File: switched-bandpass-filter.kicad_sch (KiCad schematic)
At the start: 12 parts, among them J1 SMA, J10 F3 out, J11 F4 out, J2 SMA, J3 F4 in, J4 Conn_01x06_Pin, J5 F3 in, J6 F2 in, J7 F1 in, J8 F1 out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

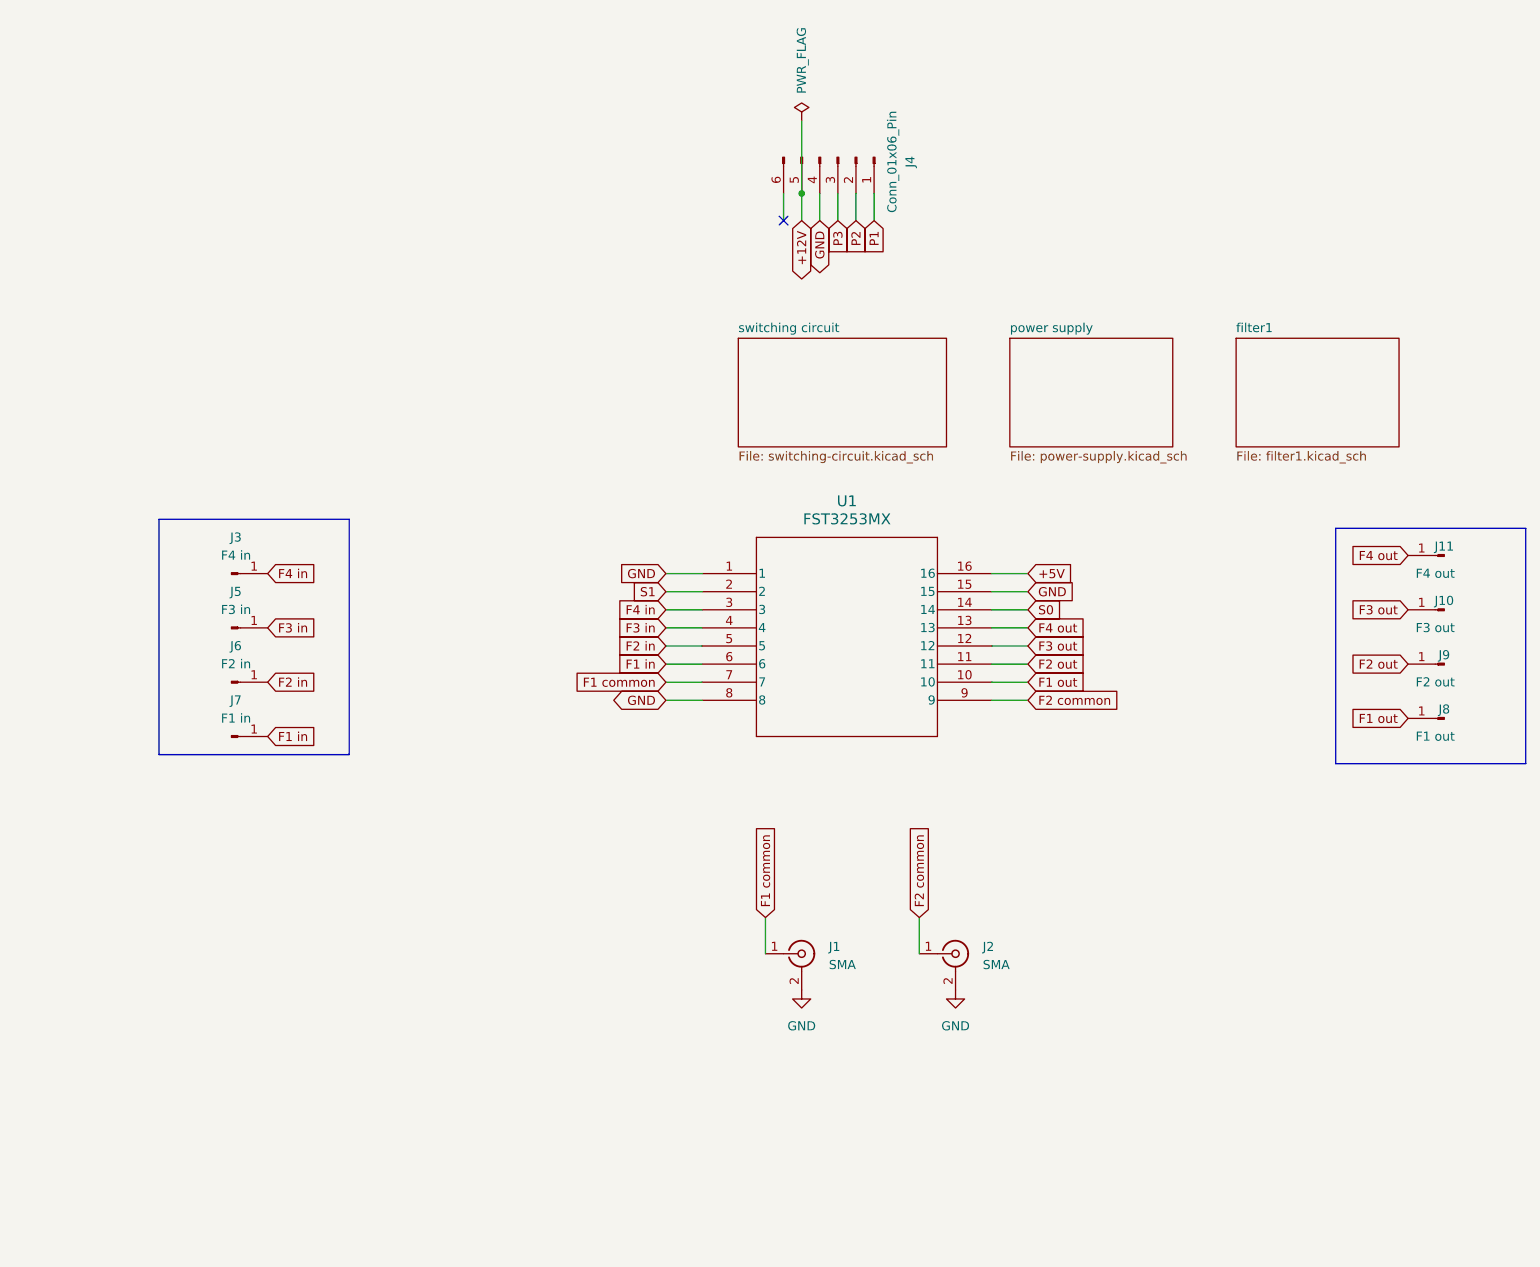
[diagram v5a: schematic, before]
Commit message: v0.4 ERC/DRC pass; added missing caps; mounting holes; moved SMA & headers out and re-spaced filter chains
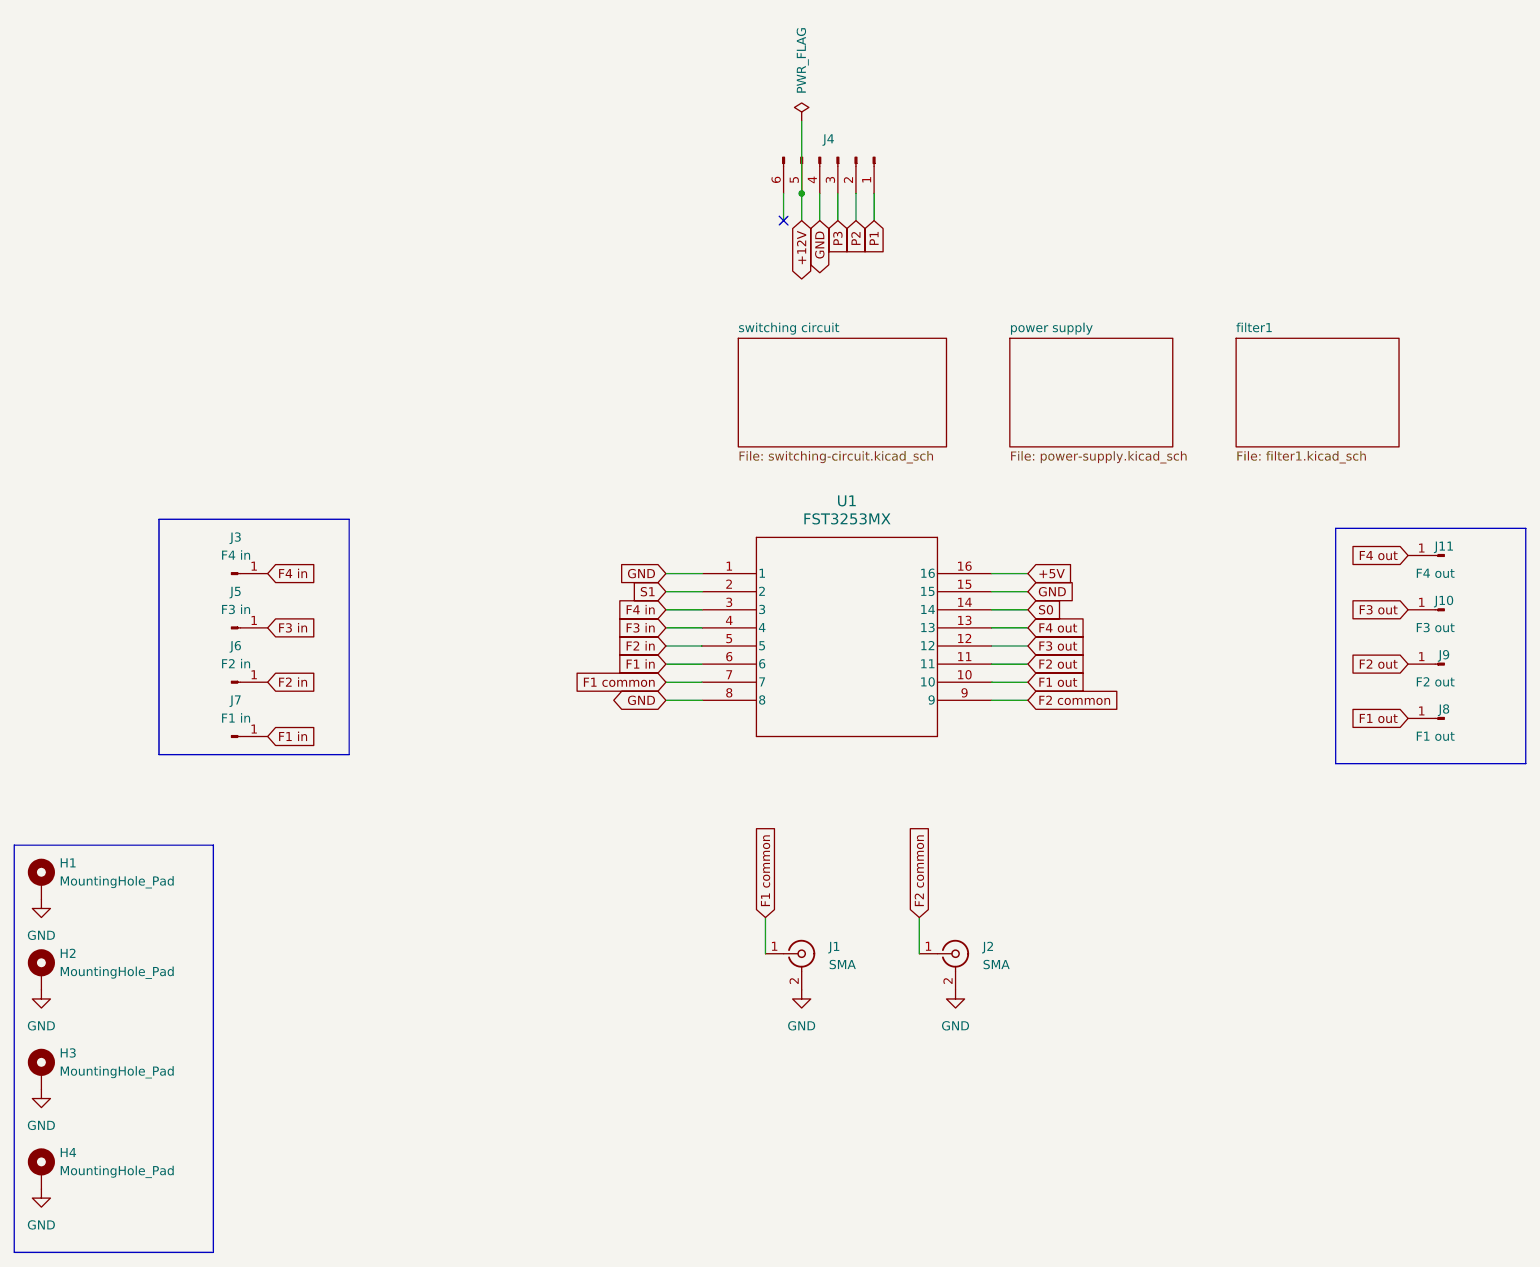
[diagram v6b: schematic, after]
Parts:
- added H1, H2, H3, H4: MountingHole_Pad, MountingHole:MountingHole_3.2mm_M3_Pad_Via, symbol Mechanical:MountingHole_Pad
- J4: value Conn_01x06_Pin -> (none)
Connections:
- net GND: now also H1.1, H2.1, H3.1, H4.1
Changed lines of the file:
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@@
     (title "switched bandpass filter")
     (date "2023-07-22")
-    (rev "v0.3")
+    (rev "v0.4")
     (comment 1 "Copyright © 2023 WA7GIL")
   )
@@
     (fill (type none))
   )
+  (rectangle (start 24.13 129.54) (end 52.07 186.69)
+    (stroke (width 0) (type default))
+    (fill (type none))
+  )
   (global_label "F1 out" (shape input) (at 219.71 111.76 180) (fields_autoplaced)
     (effects (font (size 1.27 1.27)) (justify right))
@@
         (path "/05f50450-de9a-44de-96d4-4a146d783d83/d4245743-3101-4aa9-985f-bdd1e5cf8eb9"
           (reference "#FLG08") (unit 1)
+        )
+      )
+    )
+  )
+  (symbol (lib_id "power:GND") (at 27.94 149.86 0) (unit 1)
+    (in_bom yes) (on_board yes) (dnp no) (fields_autoplaced)
+    (property "Reference" "#PWR02" (at 27.94 156.21 0)
+      (effects (font (size 1.27 1.27)) hide)
+    )
+    (property "Value" "GND" (at 27.94 154.94 0)
+      (effects (font (size 1.27 1.27)))
+    )
+    (property "Footprint" "" (at 27.94 149.86 0)
+      (effects (font (size 1.27 1.27)) hide)
+    )
+    (property "Datasheet" "" (at 27.94 149.86 0)
+      (effects (font (size 1.27 1.27)) hide)
+    )
+    (pin "1")
+    (instances
+      (project "switched-bandpass-filter"
+        (path "/05f50450-de9a-44de-96d4-4a146d783d83"
+          (reference "#PWR02") (unit 1)
+        )
+      )
+    )
+  )
+  (symbol (lib_id "power:GND") (at 27.94 163.83 0) (unit 1)
+    (in_bom yes) (on_board yes) (dnp no) (fields_autoplaced)
+    (property "Reference" "#PWR03" (at 27.94 170.18 0)
+      (effects (font (size 1.27 1.27)) hide)
+    )
+    (property "Value" "GND" (at 27.94 168.91 0)
+      (effects (font (size 1.27 1.27)))
+    )
+    (property "Footprint" "" (at 27.94 163.83 0)
+      (effects (font (size 1.27 1.27)) hide)
+    )
+    (property "Datasheet" "" (at 27.94 163.83 0)
+      (effects (font (size 1.27 1.27)) hide)
+    )
+    (pin "1")
+    (instances
+      (project "switched-bandpass-filter"
+        (path "/05f50450-de9a-44de-96d4-4a146d783d83"
+          (reference "#PWR03") (unit 1)
         )
       )
@@
     )
   )
+  (symbol (lib_id "Mechanical:MountingHole_Pad") (at 27.94 175.26 0) (unit 1)
+    (in_bom yes) (on_board yes) (dnp no) (fields_autoplaced)
+    (property "Reference" "H4" (at 30.48 172.72 0)
+      (effects (font (size 1.27 1.27)) (justify left))
+    )
+    (property "Value" "MountingHole_Pad" (at 30.48 175.26 0)
+      (effects (font (size 1.27 1.27)) (justify left))
+    )
+    (property "Footprint" "MountingHole:MountingHole_3.2mm_M3_Pad_Via" (at 27.94 175.26 0)
+      (effects (font (size 1.27 1.27)) hide)
+    )
+    (property "Datasheet" "~" (at 27.94 175.26 0)
+      (effects (font (size 1.27 1.27)) hide)
+    )
+    (pin "1")
+    (instances
+      (project "switched-bandpass-filter"
+        (path "/05f50450-de9a-44de-96d4-4a146d783d83"
+          (reference "H4") (unit 1)
+        )
+      )
+    )
+  )
   (symbol (lib_id "Connector:Conn_01x06_Pin") (at 139.7 33.02 270) (unit 1)
     (in_bom yes) (on_board yes) (dnp no) (fields_autoplaced)
-    (property "Reference" "J4" (at 149.86 33.655 0)
-      (effects (font (size 1.27 1.27)))
-    )
-    (property "Value" "Conn_01x06_Pin" (at 147.32 33.655 0)
-      (effects (font (size 1.27 1.27)))
+    (property "Reference" "J4" (at 138.43 30.48 90)
+      (effects (font (size 1.27 1.27)))
+    )
+    (property "Value" " " (at 147.32 33.655 0)
+      (effects (font (size 1.27 1.27)) hide)
     )
     (property "Footprint" "Connector_PinHeader_2.54mm:PinHeader_1x06_P2.54mm_Vertical" (at 139.7 33.02 0)
@@
     )
   )
+  (symbol (lib_id "power:GND") (at 27.94 177.8 0) (unit 1)
+    (in_bom yes) (on_board yes) (dnp no) (fields_autoplaced)
+    (property "Reference" "#PWR04" (at 27.94 184.15 0)
+      (effects (font (size 1.27 1.27)) hide)
+    )
+    (property "Value" "GND" (at 27.94 182.88 0)
+      (effects (font (size 1.27 1.27)))
+    )
+    (property "Footprint" "" (at 27.94 177.8 0)
+      (effects (font (size 1.27 1.27)) hide)
+    )
+    (property "Datasheet" "" (at 27.94 177.8 0)
+      (effects (font (size 1.27 1.27)) hide)
+    )
+    (pin "1")
+    (instances
+      (project "switched-bandpass-filter"
+        (path "/05f50450-de9a-44de-96d4-4a146d783d83"
+          (reference "#PWR04") (unit 1)
+        )
+      )
+    )
+  )
+  (symbol (lib_id "power:GND") (at 27.94 137.16 0) (unit 1)
+    (in_bom yes) (on_board yes) (dnp no) (fields_autoplaced)
+    (property "Reference" "#PWR01" (at 27.94 143.51 0)
+      (effects (font (size 1.27 1.27)) hide)
+    )
+    (property "Value" "GND" (at 27.94 142.24 0)
+      (effects (font (size 1.27 1.27)))
+    )
+    (property "Footprint" "" (at 27.94 137.16 0)
+      (effects (font (size 1.27 1.27)) hide)
+    )
+    (property "Datasheet" "" (at 27.94 137.16 0)
+      (effects (font (size 1.27 1.27)) hide)
+    )
+    (pin "1")
+    (instances
+      (project "switched-bandpass-filter"
+        (path "/05f50450-de9a-44de-96d4-4a146d783d83"
+          (reference "#PWR01") (unit 1)
+        )
+      )
+    )
+  )
   (symbol (lib_id "Connector:Conn_01x01_Pin") (at 54.61 114.3 0) (unit 1)
     (in_bom yes) (on_board yes) (dnp no) (fields_autoplaced)
@@
     )
   )
+  (symbol (lib_id "Mechanical:MountingHole_Pad") (at 27.94 161.29 0) (unit 1)
+    (in_bom yes) (on_board yes) (dnp no) (fields_autoplaced)
+    (property "Reference" "H3" (at 30.48 158.75 0)
+      (effects (font (size 1.27 1.27)) (justify left))
+    )
+    (property "Value" "MountingHole_Pad" (at 30.48 161.29 0)
+      (effects (font (size 1.27 1.27)) (justify left))
+    )
+    (property "Footprint" "MountingHole:MountingHole_3.2mm_M3_Pad_Via" (at 27.94 161.29 0)
+      (effects (font (size 1.27 1.27)) hide)
+    )
+    (property "Datasheet" "~" (at 27.94 161.29 0)
+      (effects (font (size 1.27 1.27)) hide)
+    )
+    (pin "1")
+    (instances
+      (project "switched-bandpass-filter"
+        (path "/05f50450-de9a-44de-96d4-4a146d783d83"
+          (reference "H3") (unit 1)
+        )
+      )
+    )
+  )
   (symbol (lib_id "Connector:Conn_Coaxial") (at 134.62 144.78 0) (unit 1)
     (in_bom yes) (on_board yes) (dnp no) (fields_autoplaced)
@@
         (path "/05f50450-de9a-44de-96d4-4a146d783d83"
           (reference "J1") (unit 1)
+        )
+      )
+    )
+  )
+  (symbol (lib_id "Mechanical:MountingHole_Pad") (at 27.94 147.32 0) (unit 1)
+    (in_bom yes) (on_board yes) (dnp no) (fields_autoplaced)
+    (property "Reference" "H2" (at 30.48 144.78 0)
+      (effects (font (size 1.27 1.27)) (justify left))
+    )
+    (property "Value" "MountingHole_Pad" (at 30.48 147.32 0)
+      (effects (font (size 1.27 1.27)) (justify left))
+    )
+    (property "Footprint" "MountingHole:MountingHole_3.2mm_M3_Pad_Via" (at 27.94 147.32 0)
+      (effects (font (size 1.27 1.27)) hide)
+    )
+    (property "Datasheet" "~" (at 27.94 147.32 0)
+      (effects (font (size 1.27 1.27)) hide)
+    )
+    (pin "1")
+    (instances
+      (project "switched-bandpass-filter"
+        (path "/05f50450-de9a-44de-96d4-4a146d783d83"
+          (reference "H2") (unit 1)
         )
       )
@@
         )
       )
+    )
+  )
+  (symbol (lib_id "Mechanical:MountingHole_Pad") (at 27.94 134.62 0) (unit 1)
+    (in_bom yes) (on_board yes) (dnp no) (fields_autoplaced)
+    (property "Reference" "H1" (at 30.48 132.08 0)
+      (effects (font (size 1.27 1.27)) (justify left))
+    )
+    (property "Value" "MountingHole_Pad" (at 30.48 134.62 0)
+      (effects (font (size 1.27 1.27)) (justify left))
+    )
+    (property "Footprint" "MountingHole:MountingHole_3.2mm_M3_Pad_Via" (at 27.94 134.62 0)
+      (effects (font (size 1.27 1.27)) hide)
+    )
+    (property "Datasheet" "~" (at 27.94 134.62 0)
+      (effects (font (size 1.27 1.27)) hide)
+    )
+    (pin "1")
+    (instances
+      (project "switched-bandpass-filter"
+        (path "/05f50450-de9a-44de-96d4-4a146d783d83"
+          (reference "H1") (unit 1)
+        )
+      )
